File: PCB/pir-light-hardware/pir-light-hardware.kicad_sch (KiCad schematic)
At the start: 27 parts, among them Q1 AON7240, U1 M74VHC1GT08DFT2G, U2 LMV331IDCKR, U3 AS312

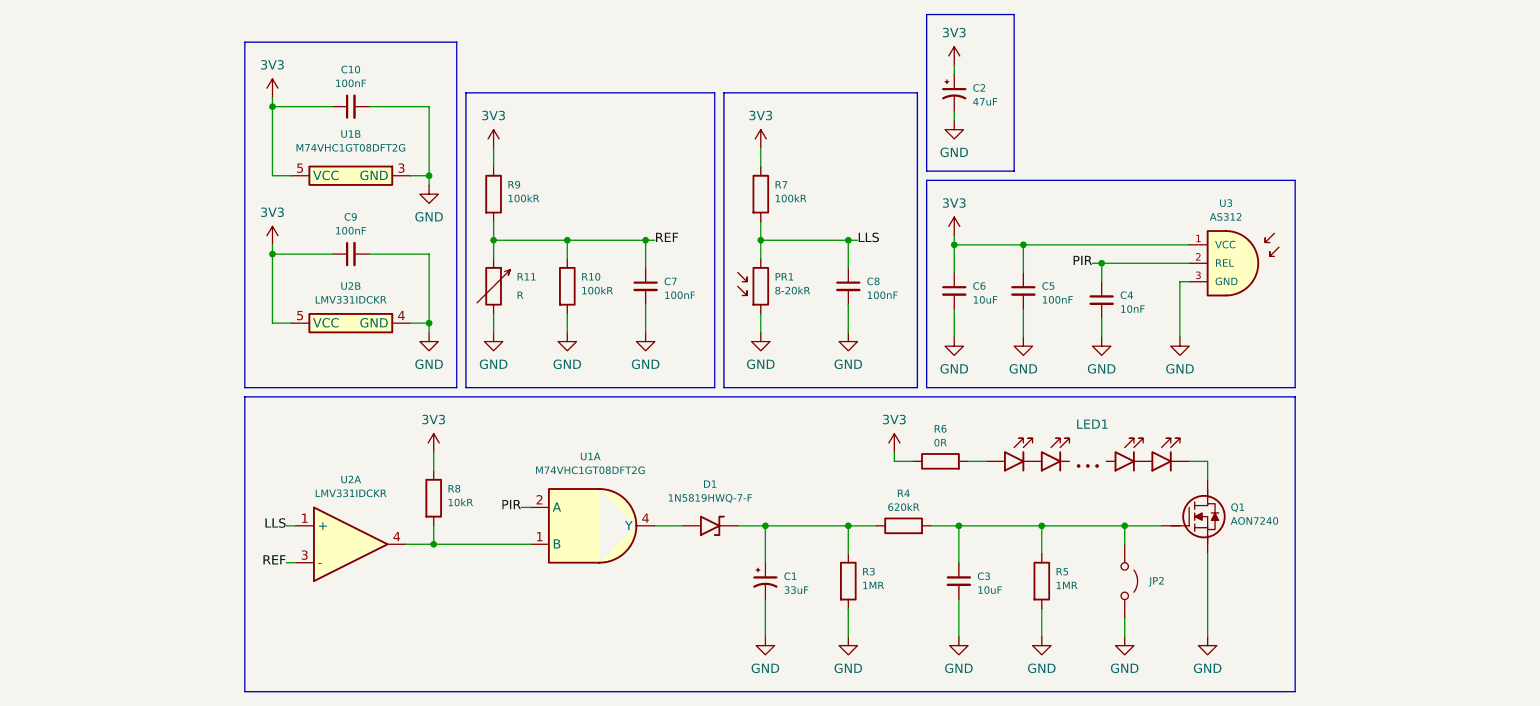
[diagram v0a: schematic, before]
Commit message: chore: add power and signal sockets
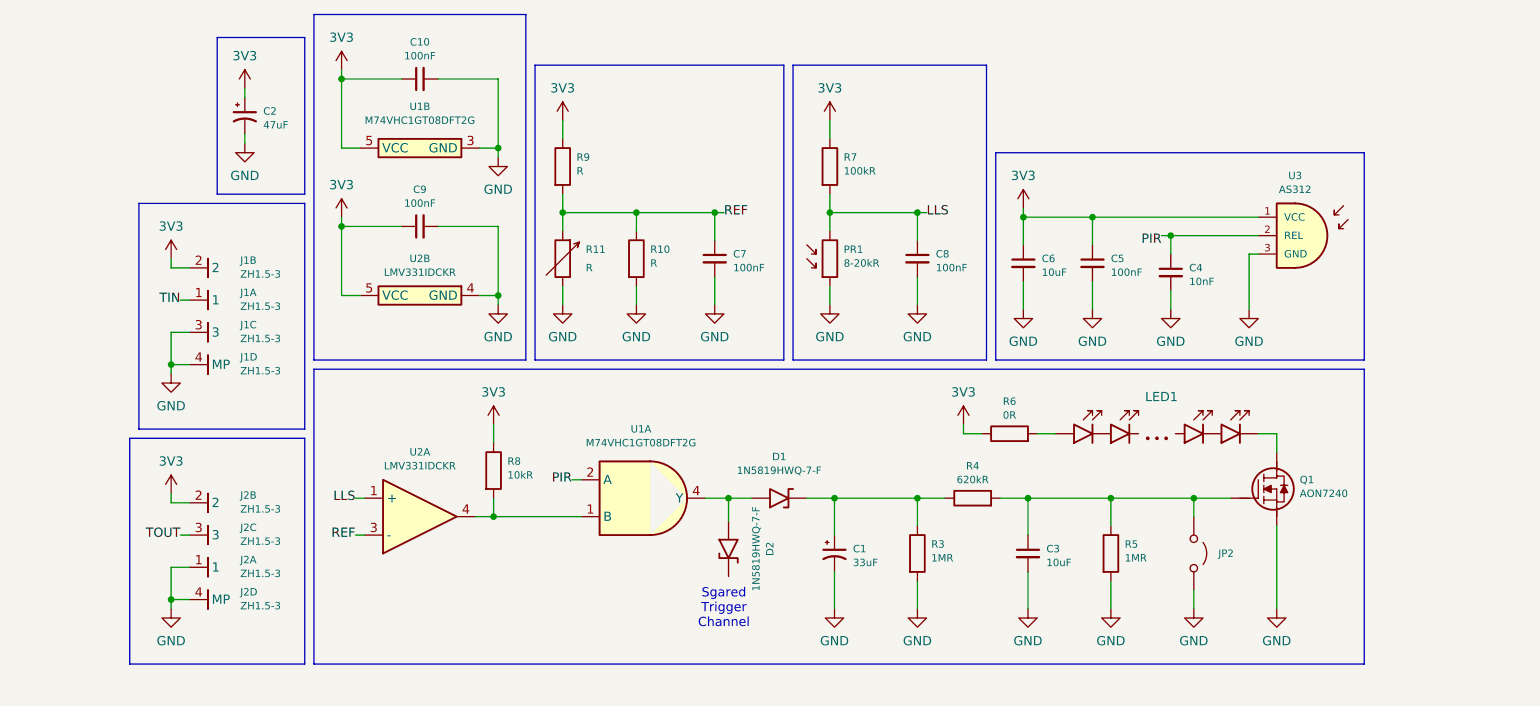
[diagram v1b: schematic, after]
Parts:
- added D2: 1N5819HWQ-7-F, 1N5819HWQ-7-F:1N5819HWQ-7-F, symbol 1N5819HWQ-7-F:1N5819HWQ-7-F
- added J1, J2: ZH1.5-3, ZH-CONNECTOR:ZH1.5-3, symbol ZH-CONNECTOR:ZH1.5-3
- C10, C4, C5, C7, C8, C9: footprint (none) -> REST:C_0402_1005Metric
- C3, C6: footprint (none) -> REST:C_0603_1608Metric
- JP2: footprint (none) -> REST:SolderJumper-2_P1.3mm_Open_RoundedPad1.0x1.5mm
- R10, R9: value 100kR -> R; footprint (none) -> REST:R_0402_1005Metric
- R3, R4, R5, R7, R8: footprint (none) -> REST:R_0402_1005Metric
- R6: footprint (none) -> REST:R_0603_1608Metric
- U1, U2: footprint SOT65P210X110-5N -> M74VHC1GT08D:SOT65P210X110-5N
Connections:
- net 3V3: now also J1.2, J2.2
- net GND: now also J1.3, J1.4 (MP), J2.1, J2.4 (MP)
- net at D1.2 (A), U1.4 (Y): now also D2.2 (A)
- new net TIN: J1.1
- new net TOUT: J2.3
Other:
- note added: "Sgared Trigger Channel"
- moved on the sheet: C1, C10, C2, C3, C4, C5, C6, C7, C8, C9, D1, JP2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

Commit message: feat: add shared trigger functionality
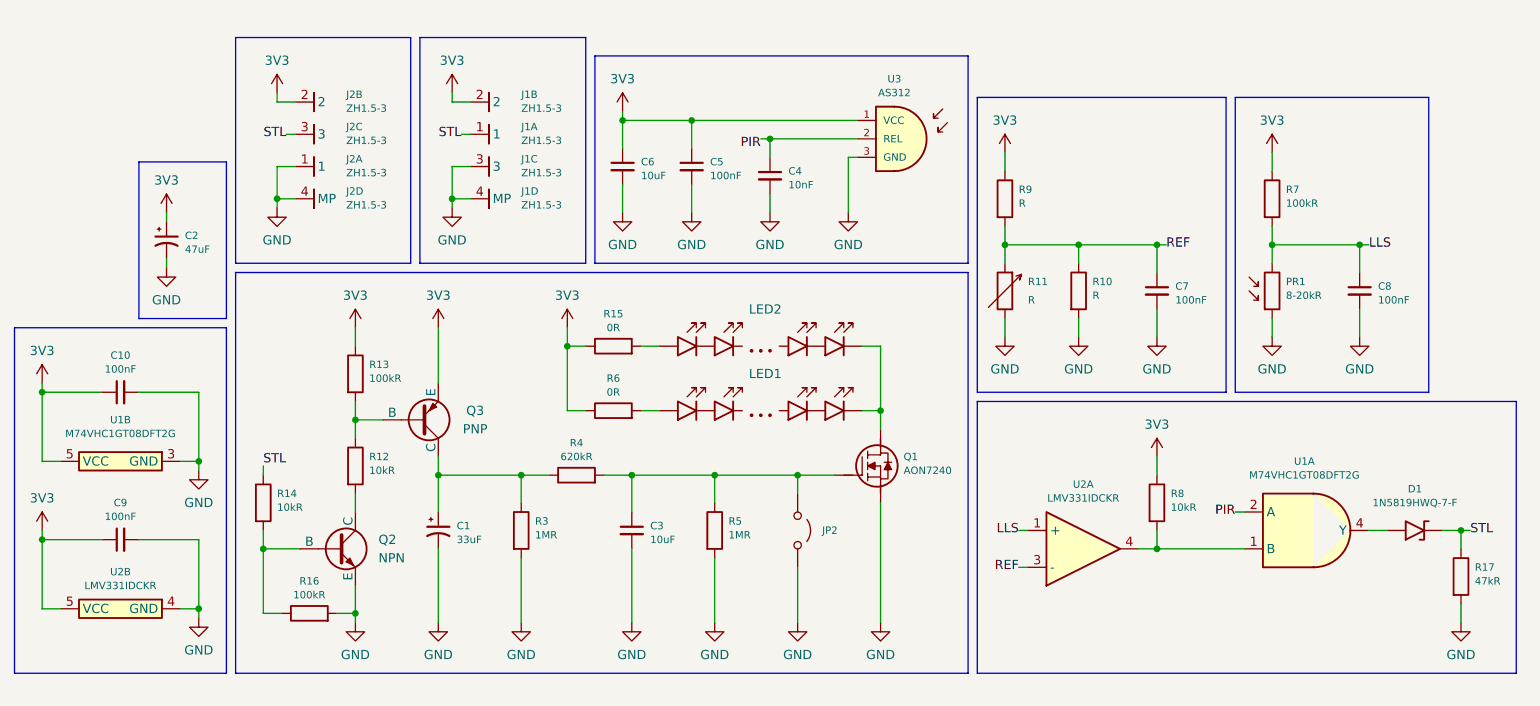
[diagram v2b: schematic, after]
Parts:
- removed D2: 1N5819HWQ-7-F, 1N5819HWQ-7-F:1N5819HWQ-7-F, symbol 1N5819HWQ-7-F:1N5819HWQ-7-F
- added LED2: (no value), LED-ROD:LED-ROD, symbol LED-ROD:LED-ROD
- added Q2: NPN, symbol Simulation_SPICE:NPN
- added Q3: PNP, symbol Simulation_SPICE:PNP
- added R12, R14: 10kR, REST:R_0402_1005Metric, symbol REST:R
- added R13, R16: 100kR, REST:R_0402_1005Metric, symbol REST:R
- added R15: 0R, REST:R_0603_1608Metric, symbol REST:R
- added R17: 47kR, REST:R_0402_1005Metric, symbol REST:R
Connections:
- net TOUT is gone; now on net STL: J2.3
- net 3V3: now also Q3.3 (E), R13.1, R15.1
- net GND: now also Q2.3 (E), R16.2, R17.2
- net at C1.1, R3.1, R4.1: now also Q3.1 (C); no longer D1.1 (K)
- net at LED1.2, Q1.3 (D): now also LED2.2
- net TIN renamed STL
- net STL: now also D1.1 (K), R14.1, R17.1
- new net: Q2.2 (B), R14.2, R16.1
- new net: LED2.1, R15.2
- new net: Q3.2 (B), R12.1, R13.2
- new net: Q2.1 (C), R12.2
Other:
- note removed: "Sgared Trigger Channel"
- moved on the sheet: C1, C10, C2, C3, C4, C5, C6, C7, C8, C9, D1, J1A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

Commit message: chore: add protection components
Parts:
- added D2: 5.1V, symbol Device:D_Zener
- added D3: D, symbol Device:D
- added F1: Fuse, symbol Device:Fuse
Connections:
- net 3V3: now also D3.1 (K), F1.2; no longer J1.2, J2.2
- net GND: now also D2.2 (A), D3.2 (A)
- net STL: now also D2.1 (K)
- new net VIN: F1.1, J1.2, J2.2
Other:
- note added: "TO CHANGE"
- moved on the sheet: C2
